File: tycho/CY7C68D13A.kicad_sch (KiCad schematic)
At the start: 25 parts, among them U1 CY7C68013A-56LTX, U2 MIC5504-3.3YM5, U8 24LC128, Y1 24 MHz

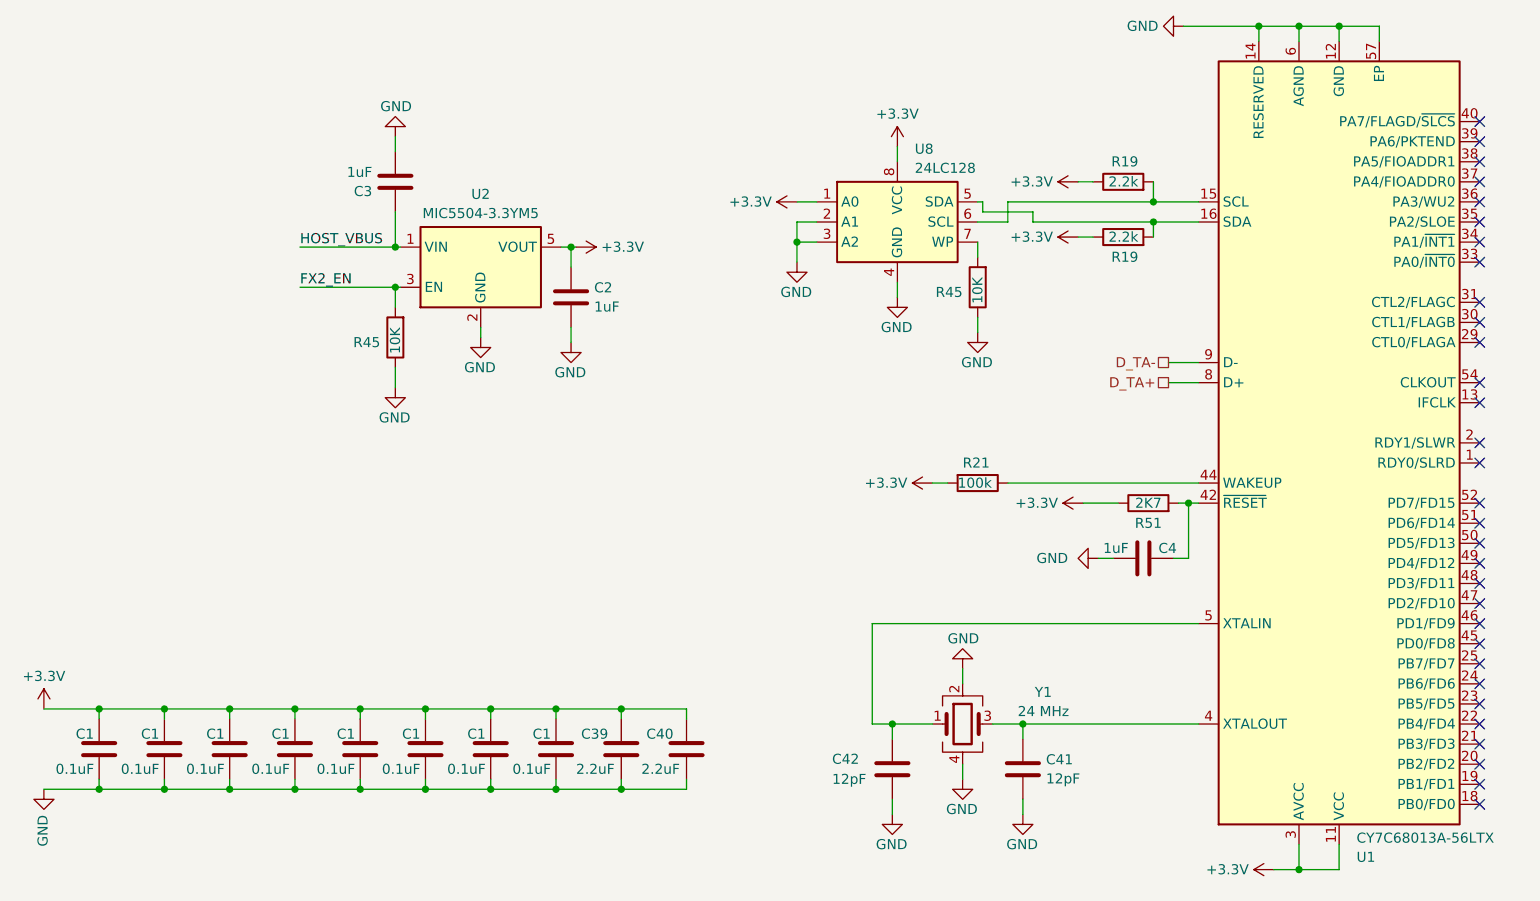
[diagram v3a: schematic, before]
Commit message: Clean up schematic including placing everything on 0.05mm grid
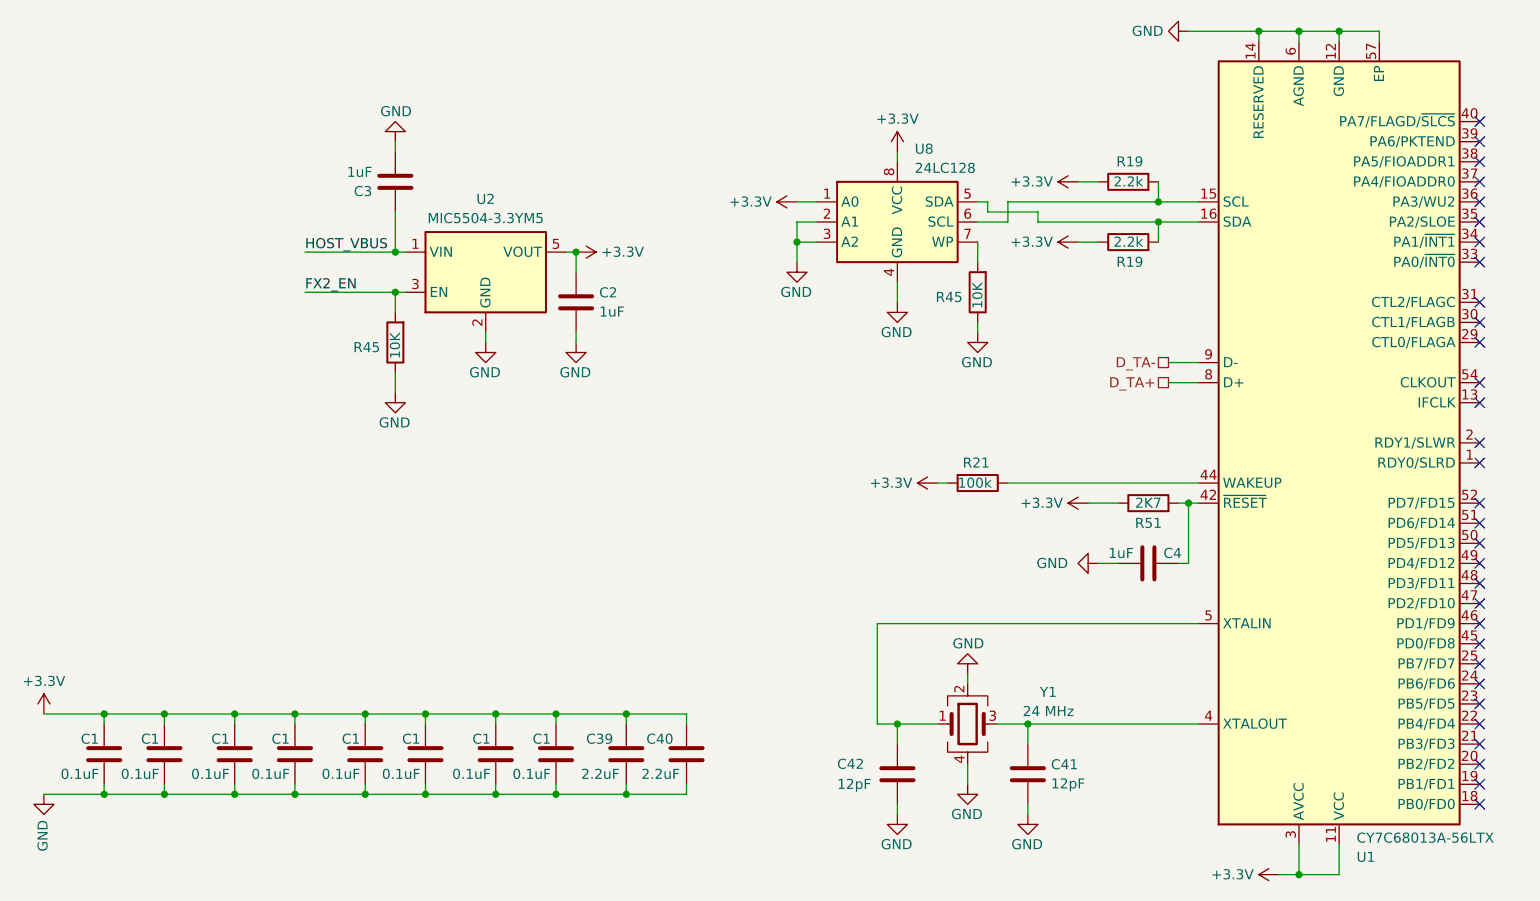
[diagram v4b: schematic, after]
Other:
- moved on the sheet: C1, C2, C39, C4, C40, C41, C42, R19, R45, U2, Y1

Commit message: ERC cleanup put everything on 0.05mm grid
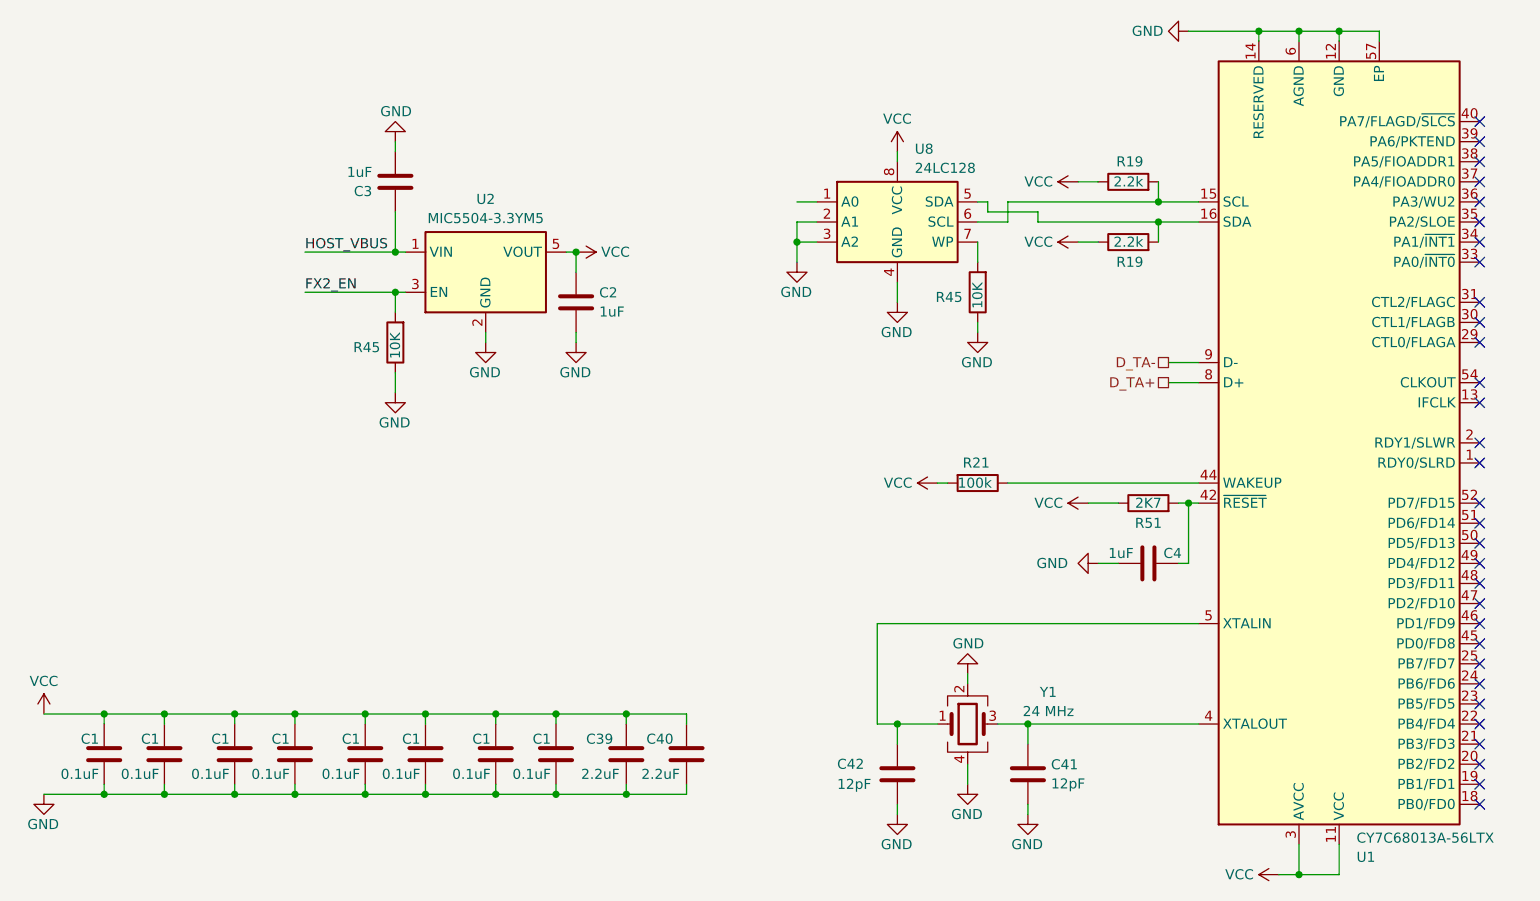
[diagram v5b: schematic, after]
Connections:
- net +3.3V renamed VCC
- net VCC: no longer U8.1 (A0)

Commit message: Fix some ERC errors
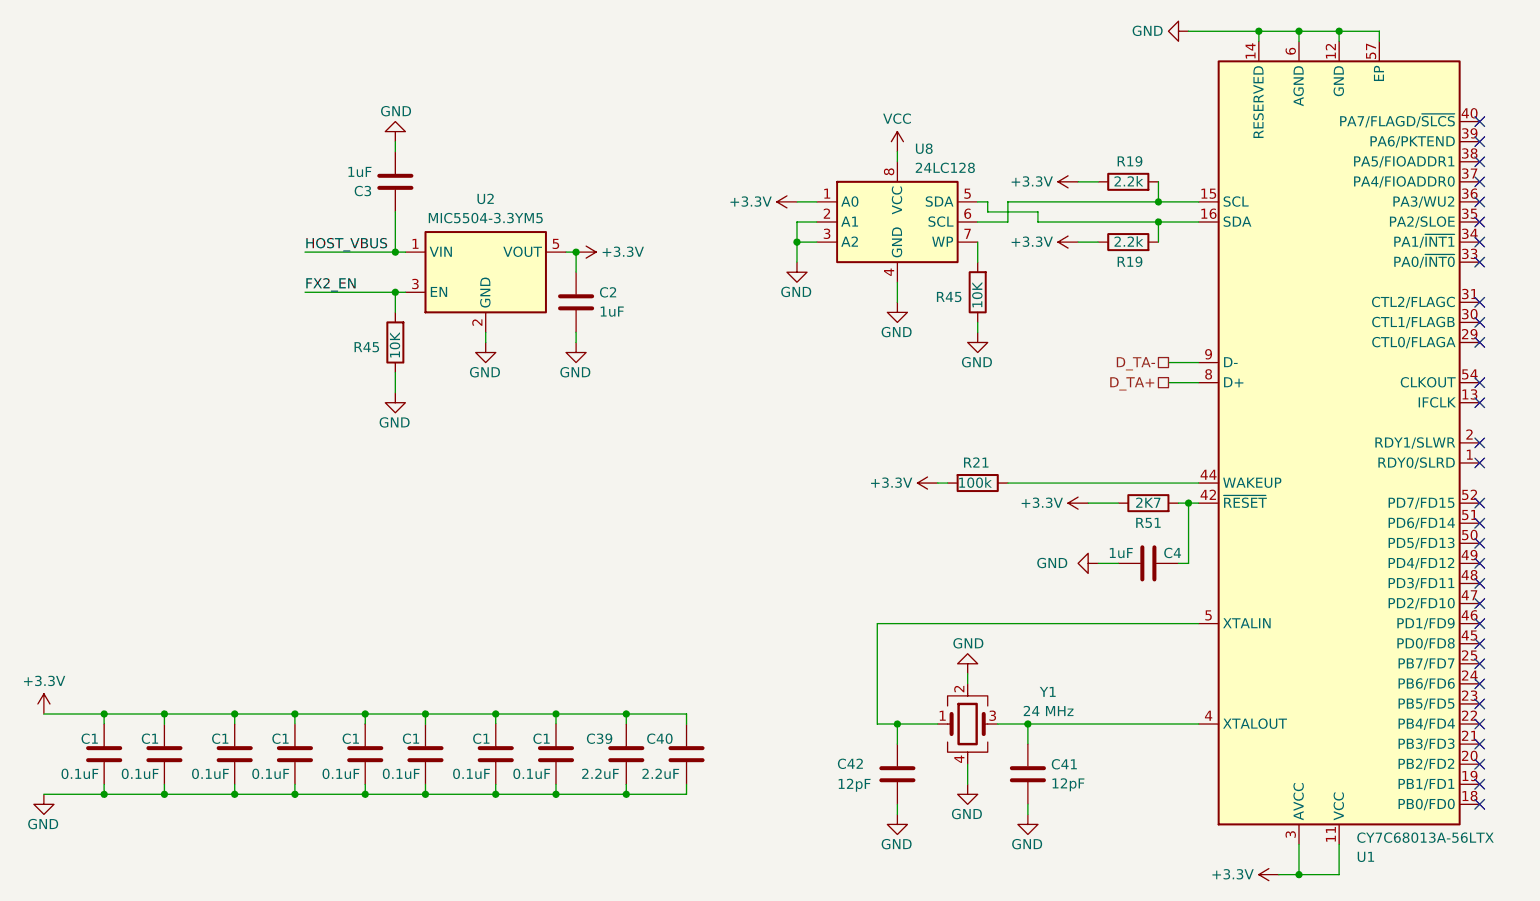
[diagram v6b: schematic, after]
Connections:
- net VCC: no longer C1.1, C1.1, C1.1, C1.1, C1.1, C1.1, C1.1, C1.1, C2.1, C39.1, C40.1, R19.1, R19.1, R21.2, R51.1, U1.11 (VCC), U1.17 (VCC), U1.27 (VCC), U1.3 (AVCC), U1.32 (VCC), U1.43 (VCC), U1.55 (VCC), U1.7 (AVCC), U2.5 (VOUT)
- net +3.3V: now reaches U8.1 (A0)
- net +3.3V: now also C1.1, C1.1, C1.1, C1.1, C1.1, C1.1, C1.1, C1.1, C2.1, C39.1, C40.1, R19.1, R19.1, R21.2, R51.1, U1.11 (VCC), U1.17 (VCC), U1.27 (VCC), U1.3 (AVCC), U1.32 (VCC), U1.43 (VCC), U1.55 (VCC), U1.7 (AVCC), U2.5 (VOUT)
